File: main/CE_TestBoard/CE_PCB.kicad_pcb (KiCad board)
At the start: 2 copper layers, 145.1 x 56.1 mm, 29 parts, among them Q1 2N2222

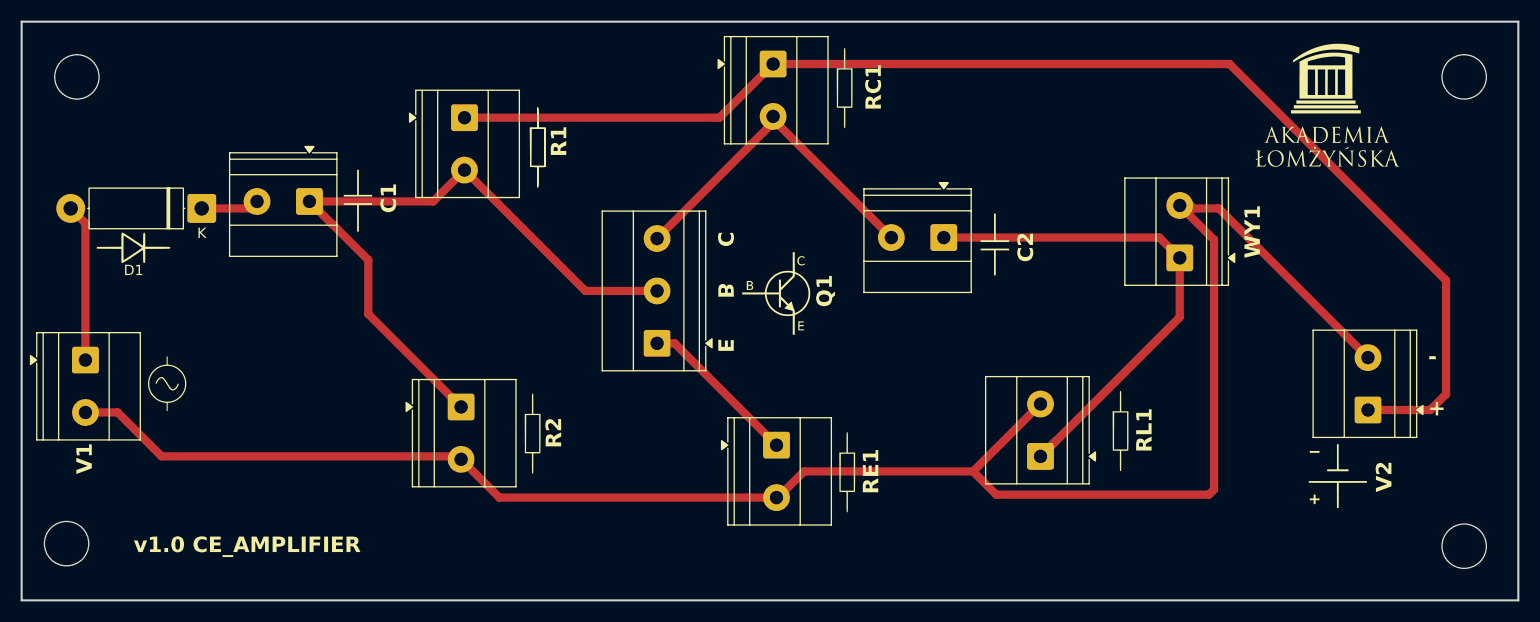
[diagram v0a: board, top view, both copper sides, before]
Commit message: Created new documents folder for Common Emitter Circuit
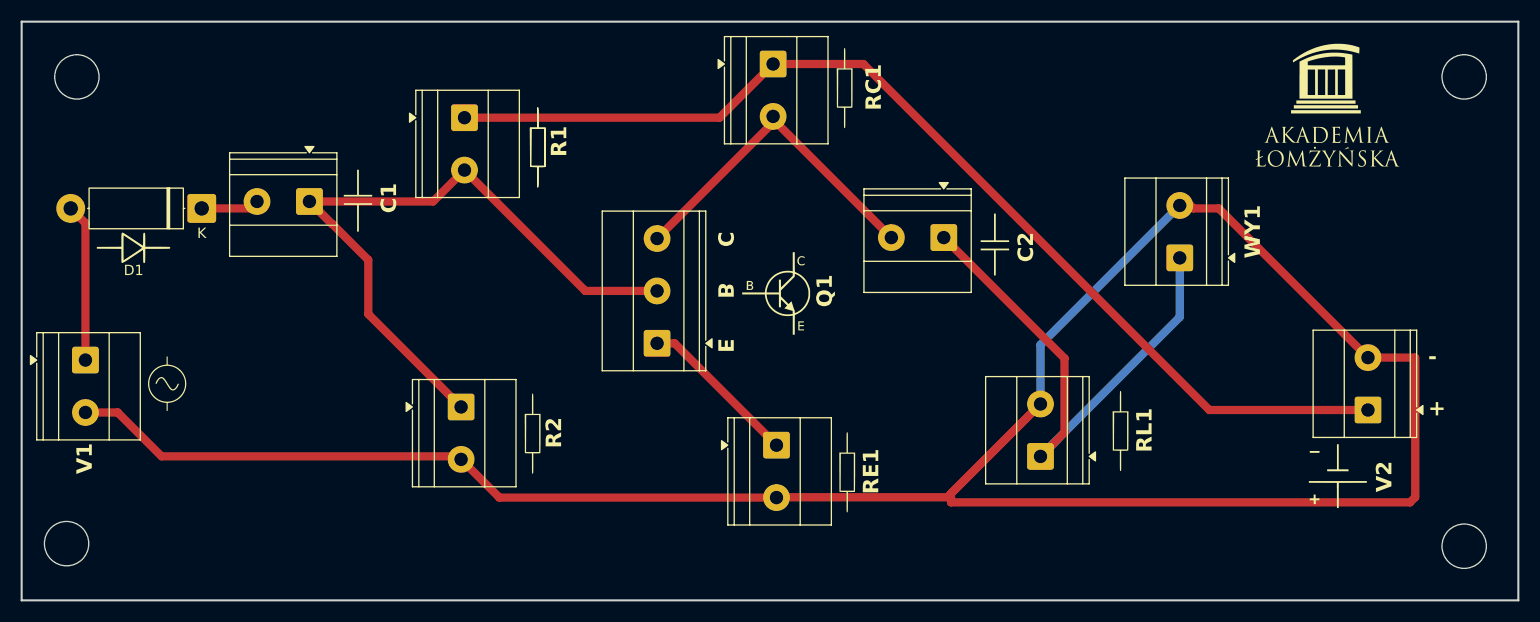
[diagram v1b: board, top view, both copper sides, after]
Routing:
- net AC: track 177.5 -> 225.4 mm
- net Net-(V2-+): track 125.2 -> 103.6 mm
- net Net-(C2-Pad1): track 50.8 -> 54.1 mm
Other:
- board text removed: "v1.0 CE_AMPLIFIER"
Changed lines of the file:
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@@
 			(outputformat 1)
 			(mirror no)
-			(drillshape 0)
+			(drillshape 1)
 			(scaleselection 1)
-			(outputdirectory "pliki wykonawcze wzmacniacz wspolny emiter/")
+			(outputdirectory "")
 		)
 	)
@@
 		)
 	)
-	(gr_text "v1.0 CE_AMPLIFIER"
-		(at 108.25 158.25 0)
-		(layer "F.SilkS")
-		(effects
-			(font
-				(size 1.5 1.5)
-				(thickness 0.3)
-				(bold yes)
-			)
-			(justify left bottom)
-		)
-	)
 	(gr_text "C"
 		(at 164.75 128.5 270)
@@
 	)
 	(segment
-		(start 170.25 110.75)
-		(end 214.5 110.75)
+		(start 165.045 115.955)
+		(end 170.25 110.75)
 		(width 0.8)
 		(layer "F.Cu")
@@
 	)
 	(segment
-		(start 233.955 144.295)
-		(end 227.9225 144.295)
+		(start 170.25 110.75)
+		(end 179 110.75)
 		(width 0.8)
 		(layer "F.Cu")
@@
 	)
 	(segment
-		(start 165.045 115.955)
-		(end 170.25 110.75)
+		(start 140.3275 115.955)
+		(end 165.045 115.955)
 		(width 0.8)
 		(layer "F.Cu")
@@
 	)
 	(segment
-		(start 235.5 142.75)
-		(end 233.955 144.295)
+		(start 179 110.75)
+		(end 212.545 144.295)
 		(width 0.8)
 		(layer "F.Cu")
@@
 	)
 	(segment
-		(start 140.3275 115.955)
-		(end 165.045 115.955)
+		(start 212.545 144.295)
+		(end 227.9225 144.295)
 		(width 0.8)
 		(layer "F.Cu")
@@
 	)
 	(segment
-		(start 214.5 110.75)
-		(end 235.5 131.75)
+		(start 211 124.75)
+		(end 213.4575 124.75)
 		(width 0.8)
 		(layer "F.Cu")
-		(net 5)
+		(net 6)
 	)
 	(segment
-		(start 235.5 131.75)
-		(end 235.5 142.75)
+		(start 196.1725 143.715)
+		(end 187.5 152.3875)
 		(width 0.8)
 		(layer "F.Cu")
-		(net 5)
+		(net 6)
 	)
 	(segment
-		(start 213 152)
-		(end 212.5 152.5)
+		(start 170.75 152.75)
+		(end 187.1375 152.75)
 		(width 0.8)
 		(layer "F.Cu")
@@
 	)
 	(segment
-		(start 173.25 150.25)
-		(end 189.6375 150.25)
+		(start 210.715 124.465)
+		(end 211 124.75)
 		(width 0.8)
 		(layer "F.Cu")
@@
 	)
 	(segment
-		(start 211 124.75)
-		(end 213.4575 124.75)
+		(start 187.5 152.3875)
+		(end 187.5 153.25)
 		(width 0.8)
 		(layer "F.Cu")
@@
 	)
 	(segment
-		(start 209.6725 124.465)
-		(end 213 127.7925)
+		(start 232.465 139.215)
+		(end 227.9225 139.215)
 		(width 0.8)
 		(layer "F.Cu")
@@
 	)
 	(segment
-		(start 210.715 124.465)
-		(end 211 124.75)
+		(start 103.5775 144.535)
+		(end 106.705 144.535)
 		(width 0.8)
 		(layer "F.Cu")
@@
 	)
 	(segment
-		(start 213 127.7925)
-		(end 213 152)
+		(start 196.1725 143.715)
+		(end 187.1375 152.75)
 		(width 0.8)
 		(layer "F.Cu")
@@
 	)
 	(segment
-		(start 170.715 152.785)
-		(end 173.25 150.25)
+		(start 170.5775 152.785)
+		(end 170.715 152.785)
 		(width 0.8)
 		(layer "F.Cu")
@@
 	)
 	(segment
-		(start 103.5775 144.535)
-		(end 106.705 144.535)
+		(start 232.5 152.75)
+		(end 232.5 139.25)
 		(width 0.8)
 		(layer "F.Cu")
@@
 	)
 	(segment
-		(start 212.5 152.5)
-		(end 191.8875 152.5)
+		(start 232.5 139.25)
+		(end 232.465 139.215)
 		(width 0.8)
 		(layer "F.Cu")
@@
 	)
 	(segment
-		(start 189.6375 150.25)
-		(end 196.1725 143.715)
+		(start 187.5 153.25)
+		(end 232 153.25)
 		(width 0.8)
 		(layer "F.Cu")
@@
 	)
 	(segment
-		(start 170.5775 152.785)
-		(end 170.715 152.785)
+		(start 170.715 152.785)
+		(end 170.75 152.75)
 		(width 0.8)
 		(layer "F.Cu")
@@
 	)
 	(segment
-		(start 191.8875 152.5)
-		(end 189.6375 150.25)
+		(start 139.705 148.785)
+		(end 140 149.08)
 		(width 0.8)
 		(layer "F.Cu")
@@
 	)
 	(segment
-		(start 139.705 148.785)
-		(end 140 149.08)
+		(start 232 153.25)
+		(end 232.5 152.75)
 		(width 0.8)
 		(layer "F.Cu")
@@
 	)
 	(segment
-		(start 209.6725 135.295)
-		(end 196.1725 148.795)
+		(start 196.1725 137.965)
+		(end 209.6725 124.465)
 		(width 0.8)
-		(layer "F.Cu")
-		(net 7)
+		(layer "B.Cu")
+		(net 6)
 	)
 	(segment
-		(start 209.6725 129.545)
-		(end 209.6725 135.295)
+		(start 196.1725 143.715)
+		(end 196.1725 137.965)
+		(width 0.8)
+		(layer "B.Cu")
+		(net 6)
+	)
+	(segment
+		(start 186.795 127.5775)
+		(end 198.5 139.2825)
 		(width 0.8)
 		(layer "F.Cu")
@@
 	)
 	(segment
-		(start 186.795 127.5775)
-		(end 207.705 127.5775)
+		(start 198.5 139.2825)
+		(end 198.5 146.4675)
 		(width 0.8)
 		(layer "F.Cu")
@@
 	)
 	(segment
-		(start 207.705 127.5775)
-		(end 209.6725 129.545)
+		(start 198.5 146.4675)
+		(end 196.1725 148.795)
 		(width 0.8)
 		(layer "F.Cu")
@@
 		(width 0.8)
 		(layer "B.Cu")
+		(net 7)
+	)
+	(segment
+		(start 209.6725 135.295)
+		(end 196.1725 148.795)
+		(width 0.8)
+		(layer "B.Cu")
+		(net 7)
+	)
+	(segment
+		(start 209.6725 129.545)
+		(end 209.6725 135.295)
+		(width 0.8)
+		(layer "B.Cu")
